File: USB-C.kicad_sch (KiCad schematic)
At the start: 9 parts, among them J2 UJC-HP-3-SMT-TR

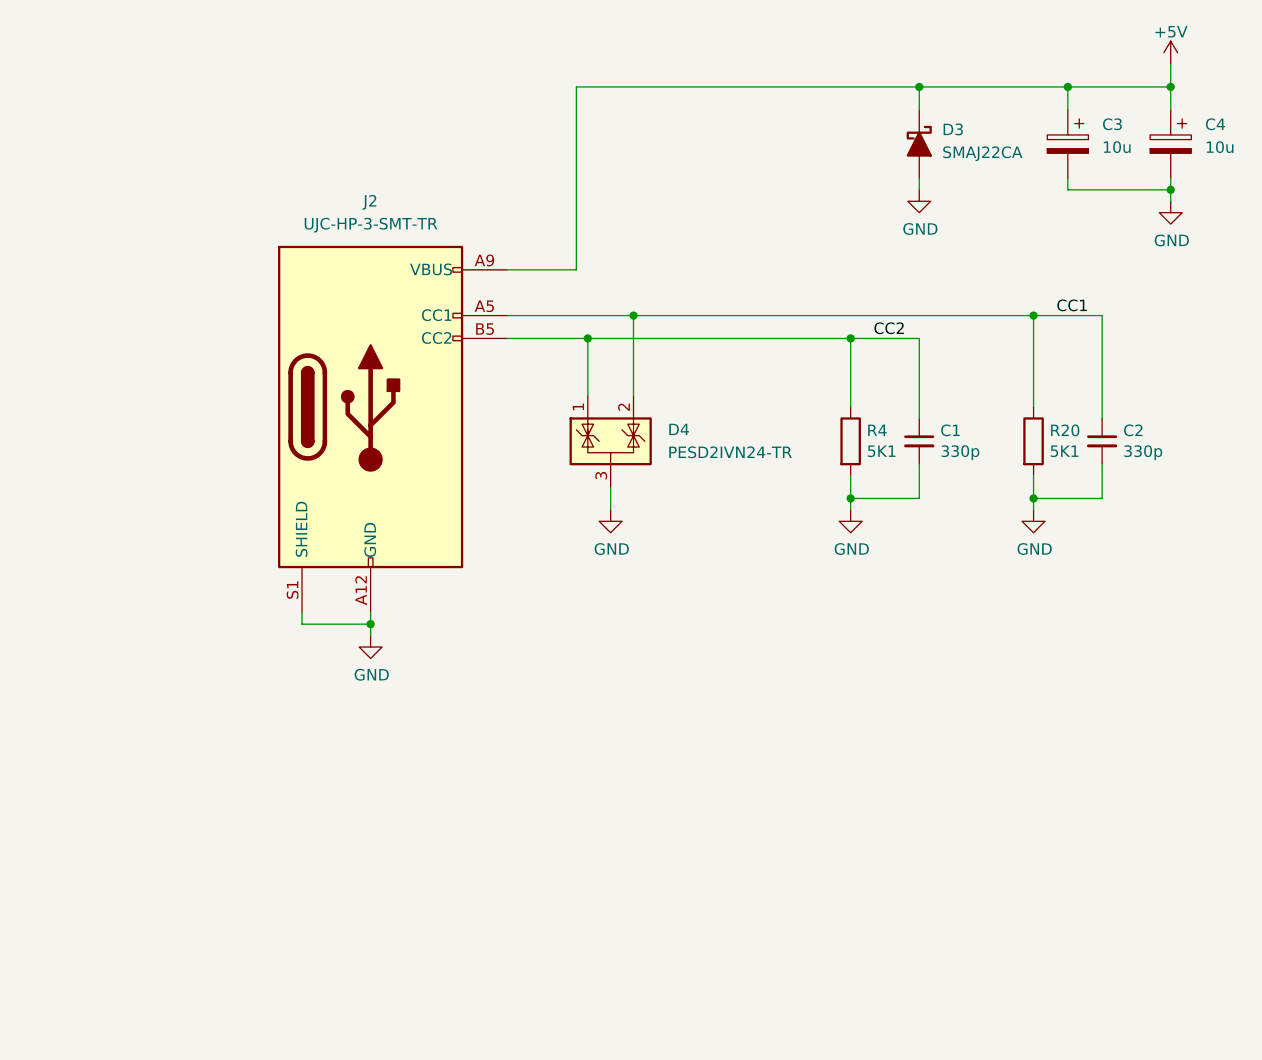
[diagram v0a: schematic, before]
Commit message: rev2 sent to fab
Added CHR RAM.
Changed board to 4 layers (was 2 layers).
Changed passives to 0603 (was 0402)
Fixed CIRAM-A10 not being hooked up
Fixed PPU-A10..A12 being hooked to VRAM but should have been.
Added more silkscreen for easier debugging.
Added filter inductor to 5V from USB-C.
Changed video out to stock (was THS7374)
Changed audio circuit to stock (was headphone amp IC)
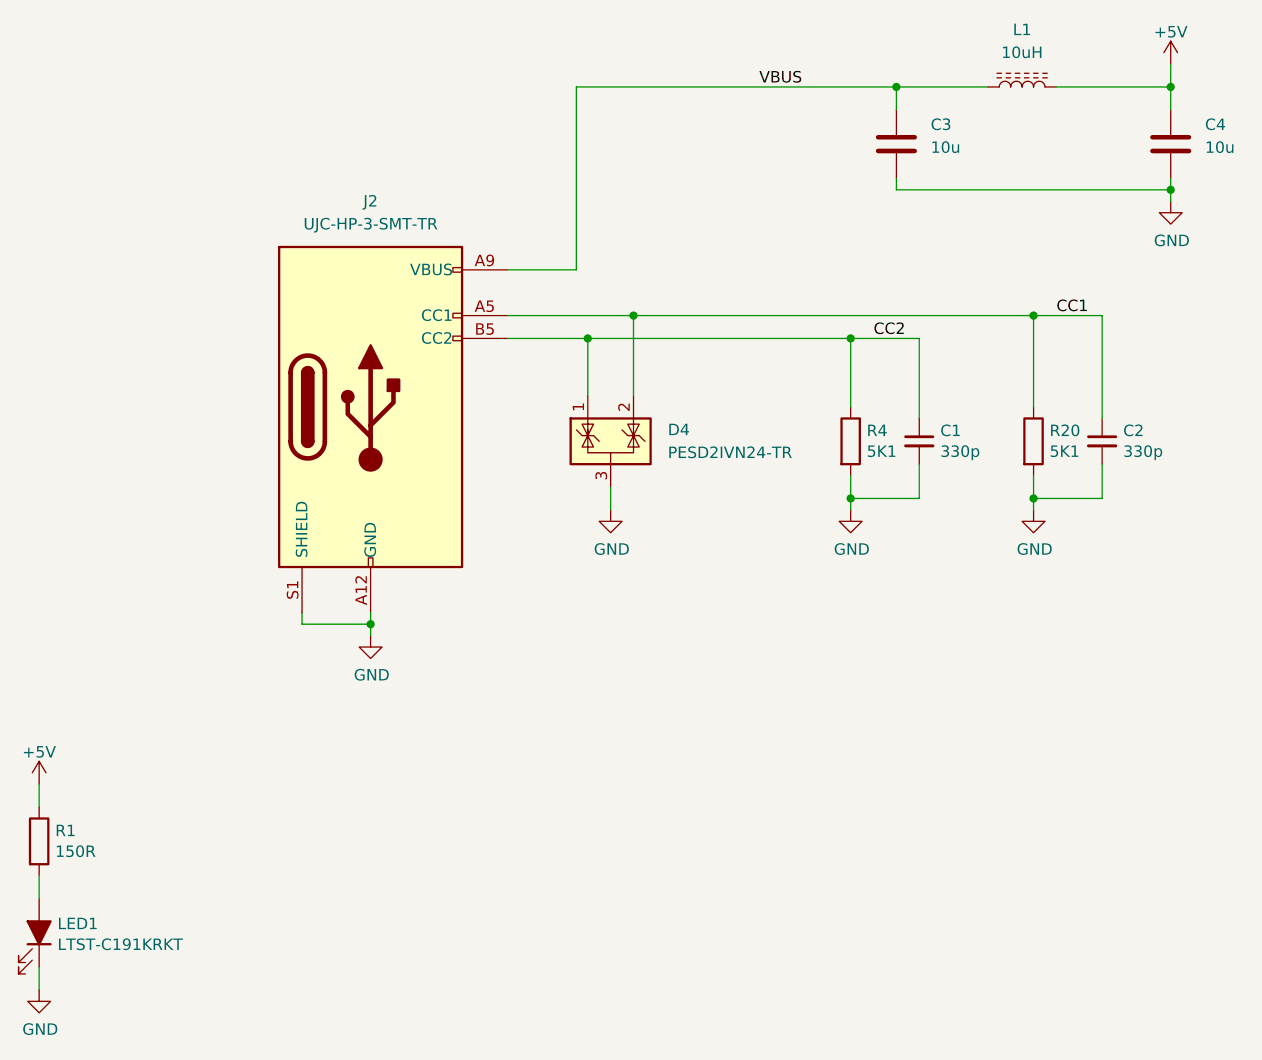
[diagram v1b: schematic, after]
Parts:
- removed D3: SMAJ22CA, Diode_SMD:D_SMA, symbol Device:D_Schottky_Filled
- added L1: 10uH, Inductor_SMD:L_Taiyo-Yuden_NR-80xx_HandSoldering, symbol Device:L_Ferrite
- added LED1: LTST-C191KRKT, LED_SMD:LED_0603_1608Metric_Pad1.05x0.95mm_HandSolder, symbol Device:LED_Filled
- added R1: 150R, Resistor_SMD:R_0603_1608Metric_Pad0.98x0.95mm_HandSolder, symbol Device:R
- C1, C2: footprint Capacitor_SMD:C_0402_1005Metric -> Capacitor_SMD:C_0603_1608Metric_Pad1.08x0.95mm_HandSolder; Digikey 1292-1308-1-ND -> (none); MPN 0402N331J500CT -> (none)
- C3, C4: footprint Capacitor_SMD:C_0805_2012Metric -> Capacitor_SMD:C_1206_3216Metric_Pad1.33x1.80mm_HandSolder; symbol Device:C_Polarized -> Device:C; Digikey 399-4925-1-ND -> (none); MPN C0805C106K8PACTU -> (none); QOH 100 -> (none)
- D4: footprint Package_TO_SOT_SMD:SOT-23 -> Package_TO_SOT_SMD:SOT-23_Handsoldering
- R20, R4: footprint Resistor_SMD:R_0402_1005Metric -> Resistor_SMD:R_0603_1608Metric_Pad0.98x0.95mm_HandSolder; Digikey 311-5.10KLRCT-ND -> (none); MPN RC0402FR-075K1L -> (none)
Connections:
- net +5V: now also L1.2, R1.1; no longer C3.1, J2.A9 (VBUS), J2.B9 (VBUS)
- net GND: now also LED1.1 (K)
- new net: LED1.2 (A), R1.2
- new net VBUS: C3.1, J2.A9 (VBUS), J2.B9 (VBUS), L1.1

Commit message: filled out BOM
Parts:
- C1, C2: Digikey (none) -> 399-C0603C331J5GAC7867CT-ND; MPN (none) -> C0603C331J5GAC7867
- C3, C4: Digikey (none) -> 1276-1075-1-ND; MPN (none) -> CL31A106KAHNNNE
- R1: Digikey (none) -> RNCP0603FTD150RCT-ND; MPN (none) -> RNCP0603FTD150R
- R20, R4: Digikey (none) -> RMCF0603FT5K10CT-ND; MPN (none) -> RMCF0603FT5K10
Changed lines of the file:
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@@
   (title_block
     (title "InGame-NES MMC3")
-    (date "2022-06-03")
-    (rev "1")
+    (date "2022-08-02")
+    (rev "2")
     (company "Late to the Game")
   )
@@
       (effects (font (size 0.762 0.762)))
     )
-    (property "Digikey" "" (id 4) (at 140.97 106.68 90)
+    (property "Digikey" "RMCF0603FT5K10CT-ND" (id 4) (at 140.97 106.68 90)
       (effects (font (size 1.524 1.524)) hide)
     )
-    (property "Description" "RES 5.1K OHM" (id 5) (at 140.97 106.68 90)
+    (property "Description" "RES SMD 5.1K OHM 1% 1/10W 0603" (id 5) (at 140.97 106.68 90)
       (effects (font (size 1.524 1.524)) hide)
     )
-    (property "MPN" "" (id 6) (at 140.97 106.68 0)
+    (property "MPN" "RMCF0603FT5K10" (id 6) (at 140.97 106.68 0)
       (effects (font (size 1.27 1.27)) hide)
     )
@@
       (effects (font (size 1.27 1.27)) hide)
     )
-    (property "Description" "CAP CER 10UF 10V X5R 0805" (id 4) (at 146.05 73.66 0)
+    (property "Description" "CAP CER 10UF 25V X5R 1206" (id 4) (at 146.05 73.66 0)
       (effects (font (size 1.27 1.27)) hide)
     )
@@
       (effects (font (size 1.27 1.27)) hide)
     )
-    (property "Digikey" "" (id 6) (at 146.05 73.66 0)
-      (effects (font (size 1.27 1.27)) hide)
-    )
-    (property "MPN" "" (id 7) (at 146.05 73.66 0)
+    (property "Digikey" "1276-1075-1-ND" (id 6) (at 146.05 73.66 0)
+      (effects (font (size 1.27 1.27)) hide)
+    )
+    (property "MPN" "CL31A106KAHNNNE" (id 7) (at 146.05 73.66 0)
       (effects (font (size 1.27 1.27)) hide)
     )
@@
       (effects (font (size 1.27 1.27)) hide)
     )
-    (property "Description" "CAP CER 10UF 10V X5R 0805" (id 4) (at 176.53 73.66 0)
+    (property "Description" "CAP CER 10UF 25V X5R 1206" (id 4) (at 176.53 73.66 0)
       (effects (font (size 1.27 1.27)) hide)
     )
@@
       (effects (font (size 1.27 1.27)) hide)
     )
-    (property "Digikey" "" (id 6) (at 176.53 73.66 0)
-      (effects (font (size 1.27 1.27)) hide)
-    )
-    (property "MPN" "" (id 7) (at 176.53 73.66 0)
+    (property "Digikey" "1276-1075-1-ND" (id 6) (at 176.53 73.66 0)
+      (effects (font (size 1.27 1.27)) hide)
+    )
+    (property "MPN" "CL31A106KAHNNNE" (id 7) (at 176.53 73.66 0)
       (effects (font (size 1.27 1.27)) hide)
     )
@@
       (effects (font (size 1.27 1.27)) hide)
     )
-    (property "Digikey" "" (id 5) (at 148.59 106.68 0)
-      (effects (font (size 1.27 1.27)) hide)
-    )
-    (property "MPN" "" (id 6) (at 148.59 106.68 0)
+    (property "Digikey" "399-C0603C331J5GAC7867CT-ND" (id 5) (at 148.59 106.68 0)
+      (effects (font (size 1.27 1.27)) hide)
+    )
+    (property "MPN" "C0603C331J5GAC7867" (id 6) (at 148.59 106.68 0)
       (effects (font (size 1.27 1.27)) hide)
     )
@@
       (effects (font (size 0.762 0.762)))
     )
-    (property "Digikey" "" (id 4) (at 50.8 151.13 90)
+    (property "Digikey" "RNCP0603FTD150RCT-ND" (id 4) (at 50.8 151.13 90)
       (effects (font (size 1.524 1.524)) hide)
     )
@@
       (effects (font (size 1.524 1.524)) hide)
     )
-    (property "MPN" "" (id 6) (at 50.8 151.13 0)
+    (property "MPN" "RNCP0603FTD150R" (id 6) (at 50.8 151.13 0)
       (effects (font (size 1.27 1.27)) hide)
     )
@@
       (effects (font (size 0.762 0.762)))
     )
-    (property "Digikey" "" (id 4) (at 161.29 106.68 90)
+    (property "Digikey" "RMCF0603FT5K10CT-ND" (id 4) (at 161.29 106.68 90)
       (effects (font (size 1.524 1.524)) hide)
     )
-    (property "Description" "RES 5.1K OHM" (id 5) (at 161.29 106.68 90)
+    (property "Description" "RES SMD 5.1K OHM 1% 1/10W 0603" (id 5) (at 161.29 106.68 90)
       (effects (font (size 1.524 1.524)) hide)
     )
-    (property "MPN" "" (id 6) (at 161.29 106.68 0)
+    (property "MPN" "RMCF0603FT5K10" (id 6) (at 161.29 106.68 0)
       (effects (font (size 1.27 1.27)) hide)
     )
@@
       (effects (font (size 1.27 1.27)) hide)
     )
-    (property "Digikey" "" (id 5) (at 168.91 106.68 0)
-      (effects (font (size 1.27 1.27)) hide)
-    )
-    (property "MPN" "" (id 6) (at 168.91 106.68 0)
-      (effects (font (size 1.27 1.27)) hide)
-    )
+    (property "Digikey" "399-C0603C331J5GAC7867CT-ND" (id 5) (at 168.91 106.68 0)
+      (effects (font (size 1.27 1.27)) hide)
+    )
+    (property "MPN" "C0603C331J5GAC7867" (id 6) (at 168.91 106.68 0)
+      (effects (font (size 1.27 1.27)) hide)
+    )
